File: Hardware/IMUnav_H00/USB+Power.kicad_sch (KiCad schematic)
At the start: 58 parts, among them IC1 TP4056, J1 918-418K2023S40001, SW1 MT-102, U1 USB2514B-AEZC-TR, U4 TPS62823DLC, U5 USBLC6-2P6, U6 TVS0500DRV, X1 SX5M24.000M20F30TNN

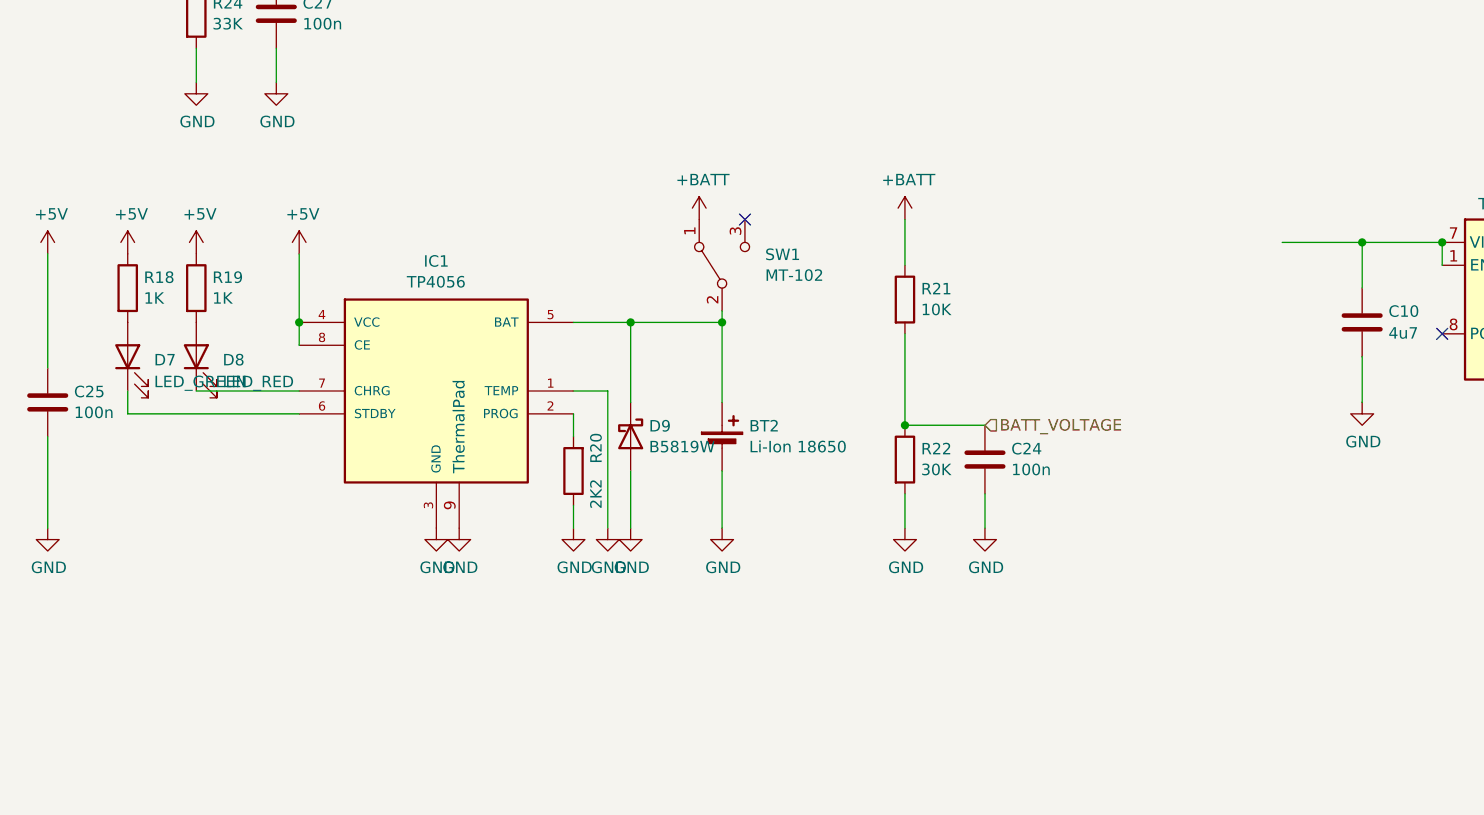
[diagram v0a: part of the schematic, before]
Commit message: Added GPS. Changes in power management.
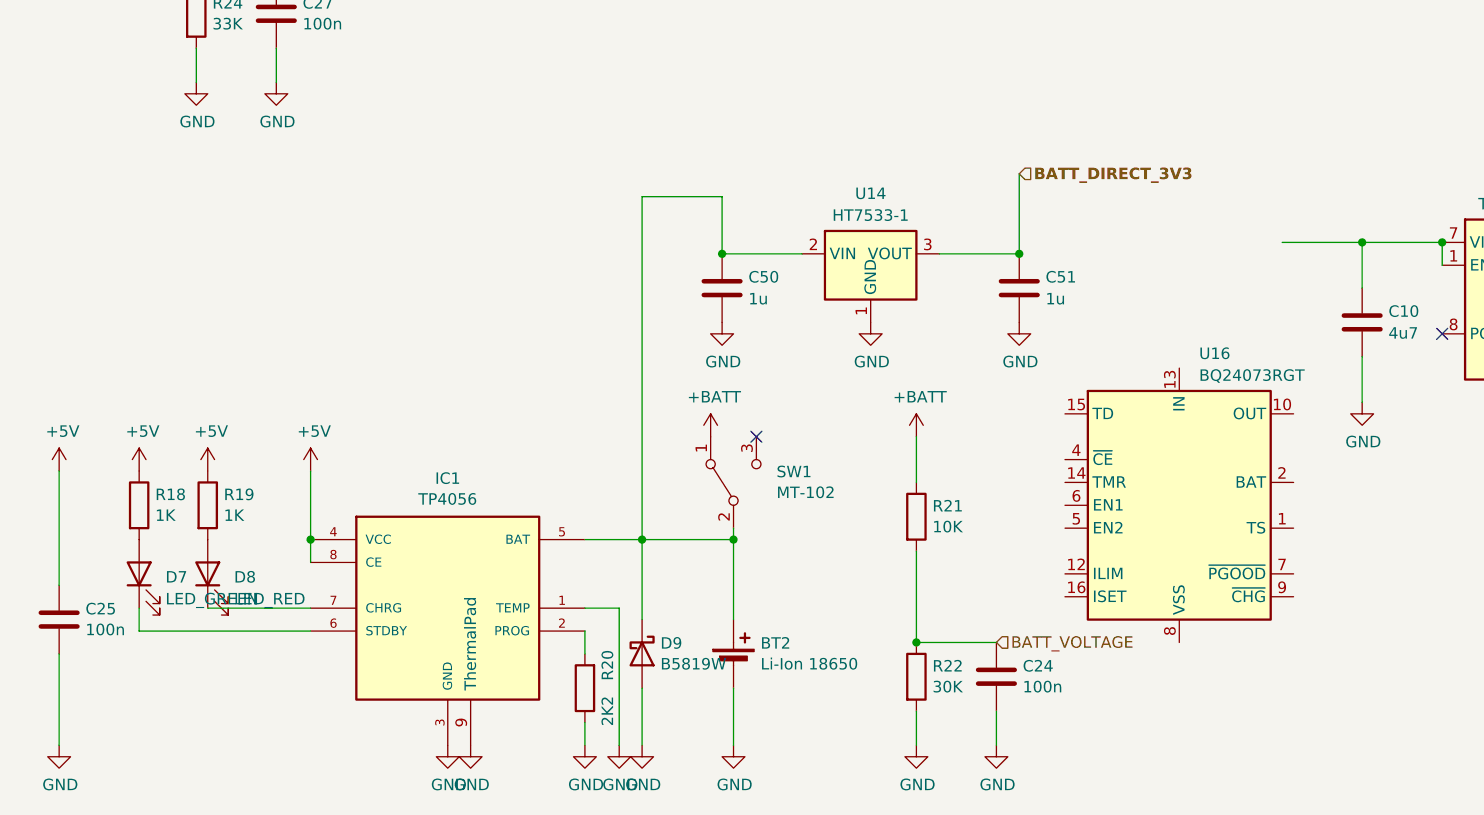
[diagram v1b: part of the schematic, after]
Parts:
- added C50, C51: 1u, Capacitor_SMD:C_0603_1608Metric, symbol Device:C
- added U14: HT7533-1, Package_TO_SOT_SMD:SOT-89-3, symbol Regulator_Linear:HT75xx-1-SOT89
- added U16: BQ24073RGT, Package_DFN_QFN:VQFN-16-1EP_3x3mm_P0.5mm_EP1.6x1.6mm, symbol Battery_Management:BQ24073RGT
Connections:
- net GND: now also C50.2, C51.2, U14.1 (GND)
- net at BT2.1 (+), D9.1 (K), IC1.5 (BAT)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: now also C50.1, U14.2 (VIN)
- new net: U16.10 (OUT), U16.11 (OUT)
- new net: U16.17 (VSS), U16.8 (VSS)
- new net: U16.2 (BAT), U16.3 (BAT)
- new net BATT_DIRECT_3V3: C51.1, U14.3 (VOUT)
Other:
- moved on the sheet: BT2, C24, C25, D7, D8, D9, IC1, R18, R19, R20, R21, R22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

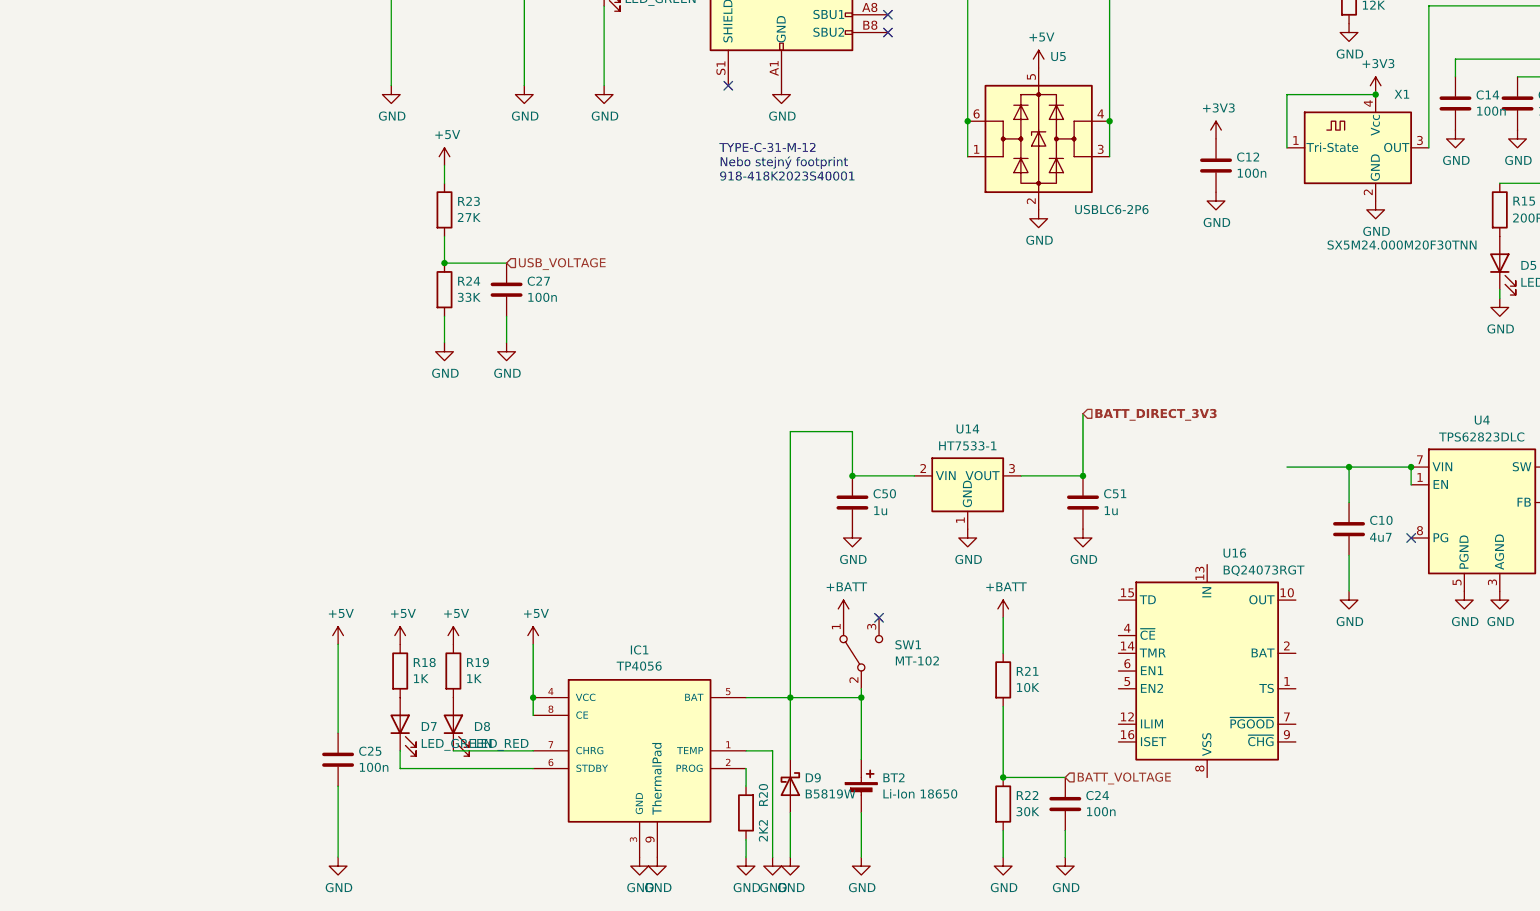
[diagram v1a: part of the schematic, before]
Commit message: Changes in power management
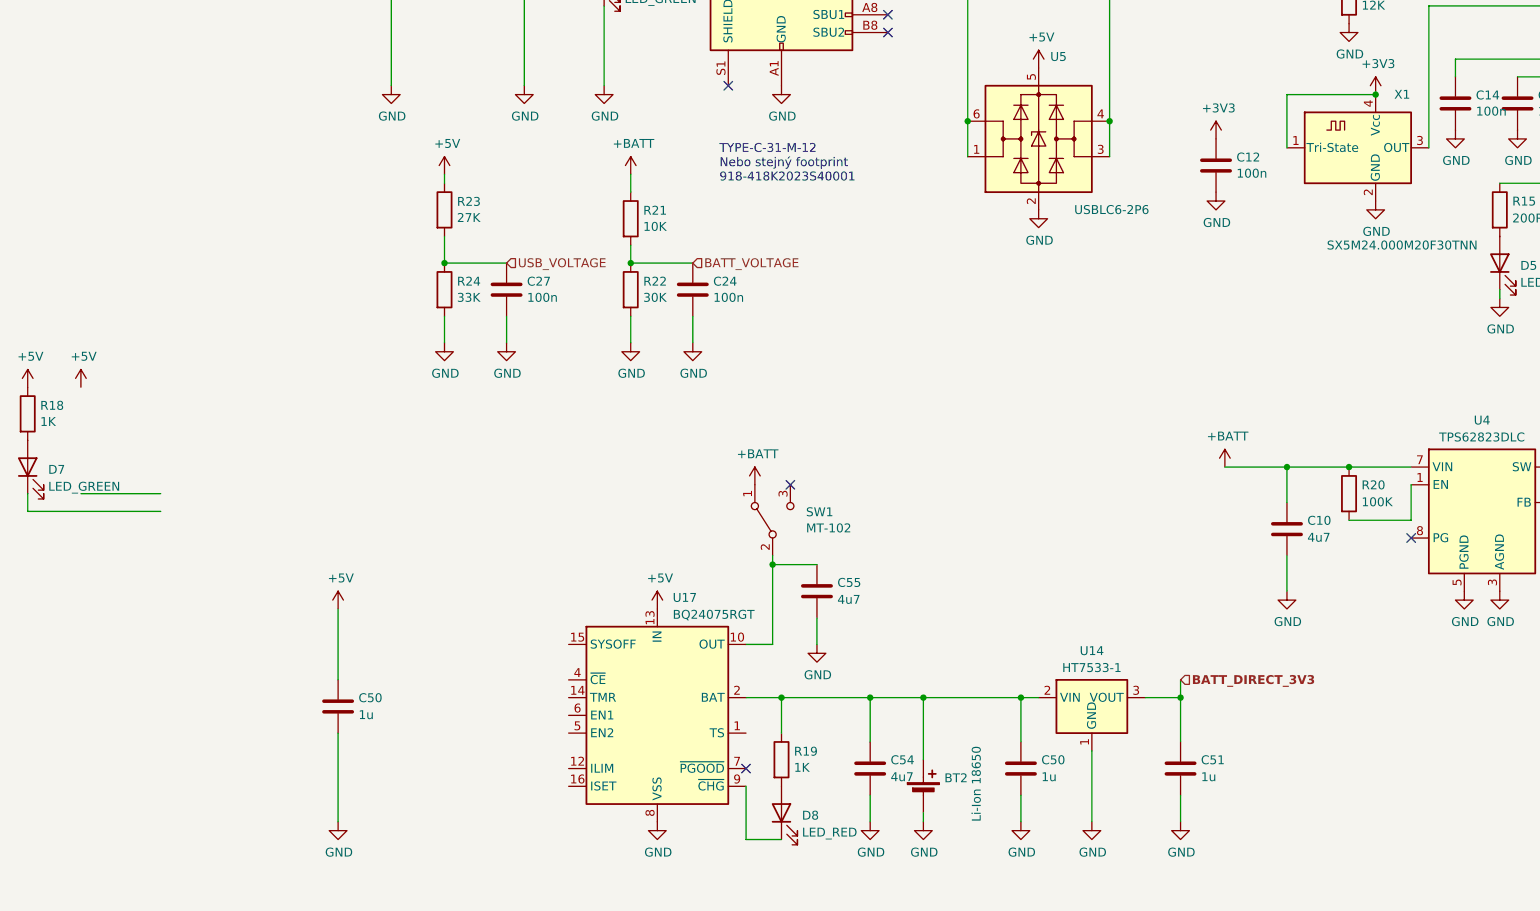
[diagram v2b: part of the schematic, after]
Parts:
- removed C25: 100n, Capacitor_SMD:C_0603_1608Metric, symbol Device:C
- removed D9: B5819W, Diode_SMD:D_SOD-123, symbol Device:D_Schottky
- removed IC1: TP4056, Package_SO:SOIC-8-1EP_3.9x4.9mm_P1.27mm_EP2.514x3.2mm_ThermalVias, symbol Sergej_Library:TP4056
- removed U16: BQ24073RGT, Package_DFN_QFN:VQFN-16-1EP_3x3mm_P0.5mm_EP1.6x1.6mm, symbol Battery_Management:BQ24073RGT
- added C50: 1u, Capacitor_SMD:C_0603_1608Metric, symbol Device:C
- added C54, C55: 4u7, Capacitor_SMD:C_0603_1608Metric, symbol Device:C
- added U17: BQ24075RGT, Package_DFN_QFN:VQFN-16-1EP_3x3mm_P0.5mm_EP1.6x1.6mm, symbol Battery_Management:BQ24075RGT
- R20: value 2K2 -> 100K; LCSC C4190 -> C25803
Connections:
- net +5V: now also C50.1, U17.13 (IN); no longer R19.1
- net +BATT: now also C10.1, R20.1, U4.7 (VIN)
- net GND: now also C50.2, C54.2, C55.2, U17.17 (VSS), U17.8 (VSS); no longer R20.1
- net at D8.1 (K): now also U17.9 (~{CHG})
- net at BT2.1 (+), C50.1, U14.2 (VIN): now also R19.1, C54.1, U17.2 (BAT), U17.3 (BAT); no longer SW1.2 (B)
- net at R20.2: now also U4.1 (EN)
- new net: C55.1, SW1.2 (B), U17.10 (OUT), U17.11 (OUT)
- no-connect marks 15 -> 16
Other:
- moved on the sheet: BT2, C10, C24, C50, C51, D7, R18, R21, R22, SW1, U14

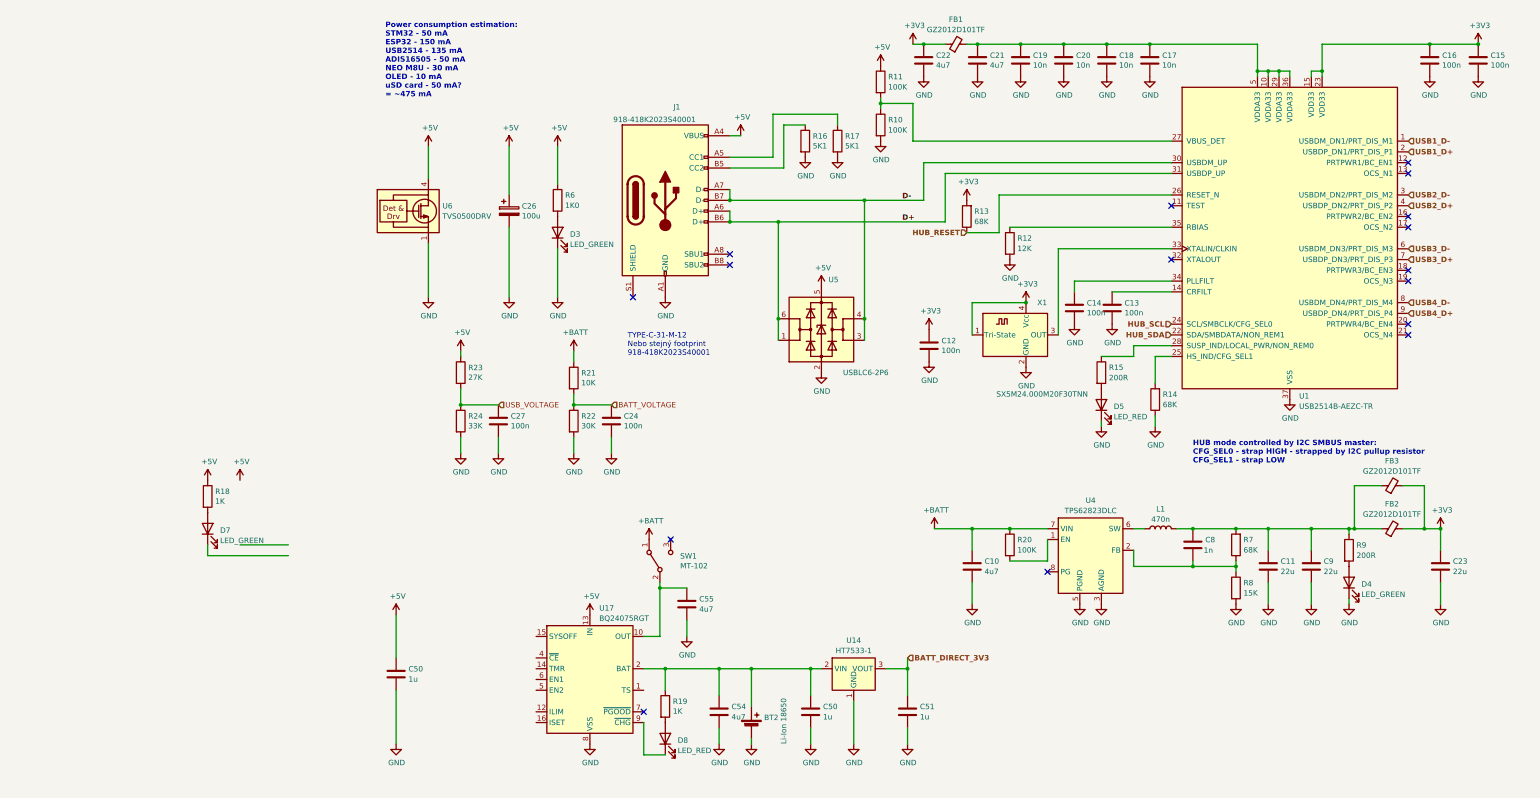
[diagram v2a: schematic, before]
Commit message: Added .gitignore for KiCad file structure
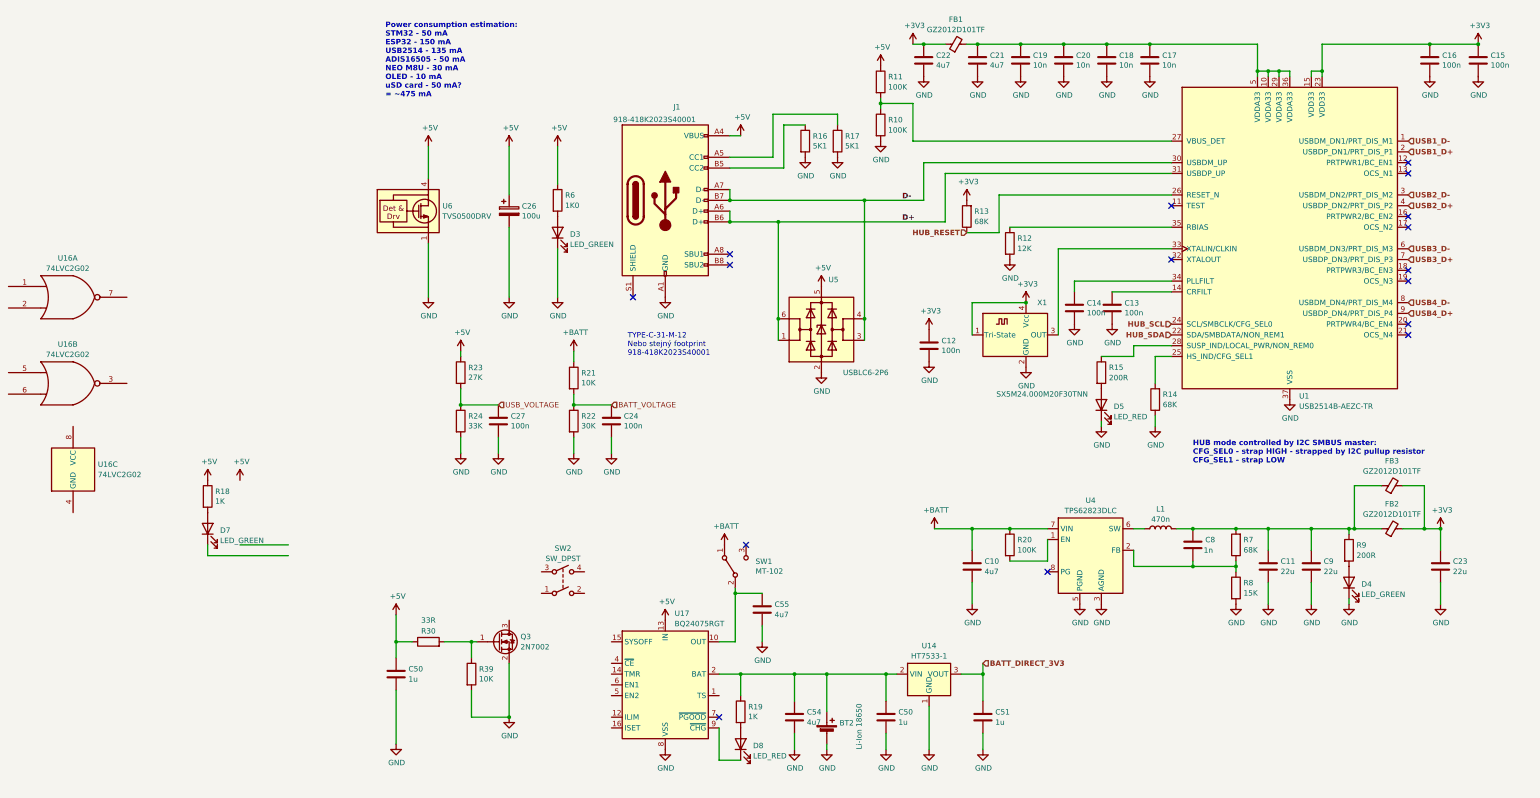
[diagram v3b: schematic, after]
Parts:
- added Q3: 2N7002, Package_TO_SOT_SMD:SOT-23, symbol Transistor_FET:2N7002
- added R30: 33R, Resistor_SMD:R_0603_1608Metric, symbol Device:R
- added R39: 10K, Resistor_SMD:R_0603_1608Metric, symbol Device:R
- added SW2: SW_DPST, symbol Switch:SW_DPST
- added U16: 74LVC2G02, symbol 74xGxx:74LVC2G02
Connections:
- net +5V: now also R30.1
- net GND: now also Q3.2 (S), R39.2
- new net: Q3.1 (G), R30.2, R39.1
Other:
- moved on the sheet: BT2, C50, C51, C54, C55, D8, R19, SW1, U14, U17
